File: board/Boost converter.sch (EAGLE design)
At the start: 21 parts, among them IC1 NE555N, IC2 attiny84, IC3 attiny85, Q1 2n7000, Q2 zvp4105

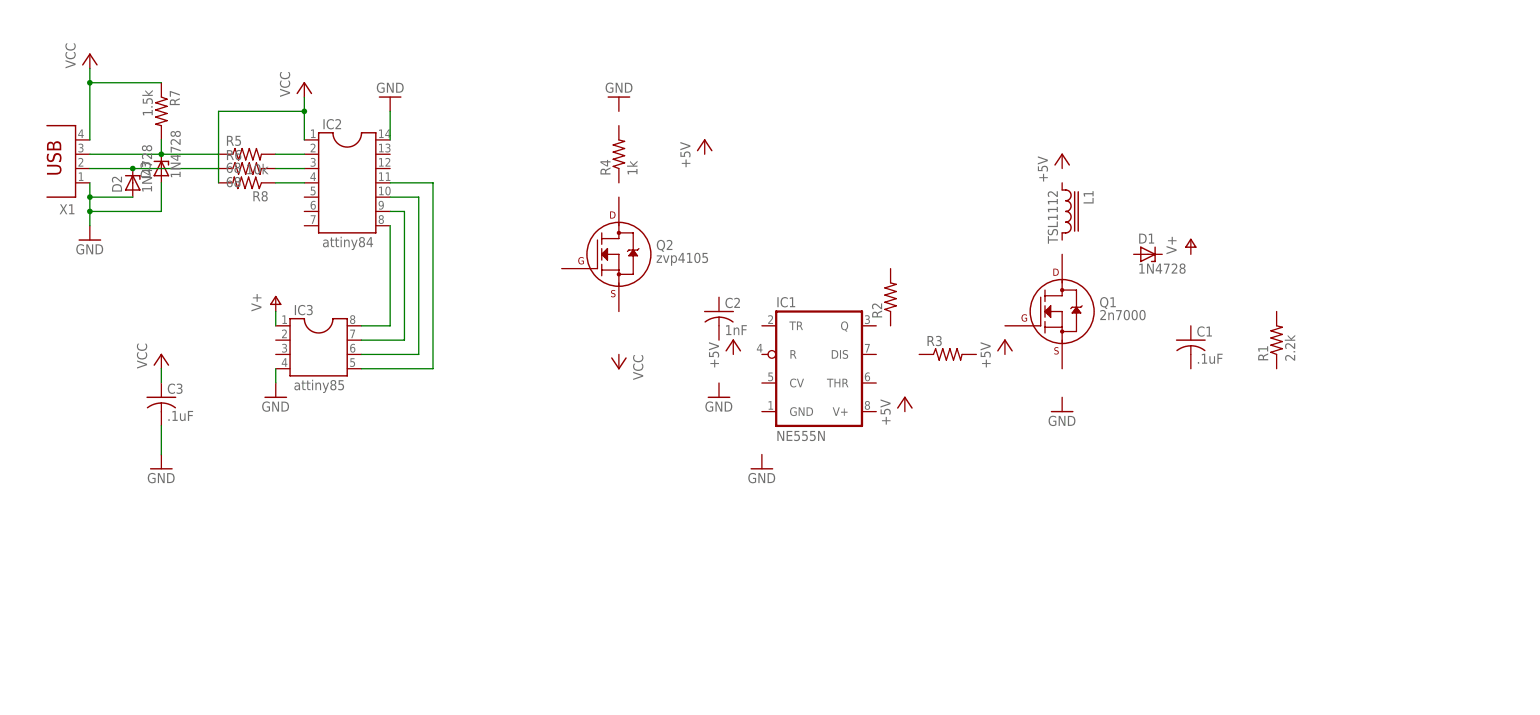
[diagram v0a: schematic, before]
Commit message: added v-usb library and done routing board
added v-usb library, but still need to change settings in usbconfig.h. also usb needs to use only one port for both d+ and d- lines (d+ can't be on pa0 and d- on pb1) so I had to change the usb data lines again. d+ is on PA0 with pcint0 and d- is on PA7. attiny85 pin 2 is now on PA6
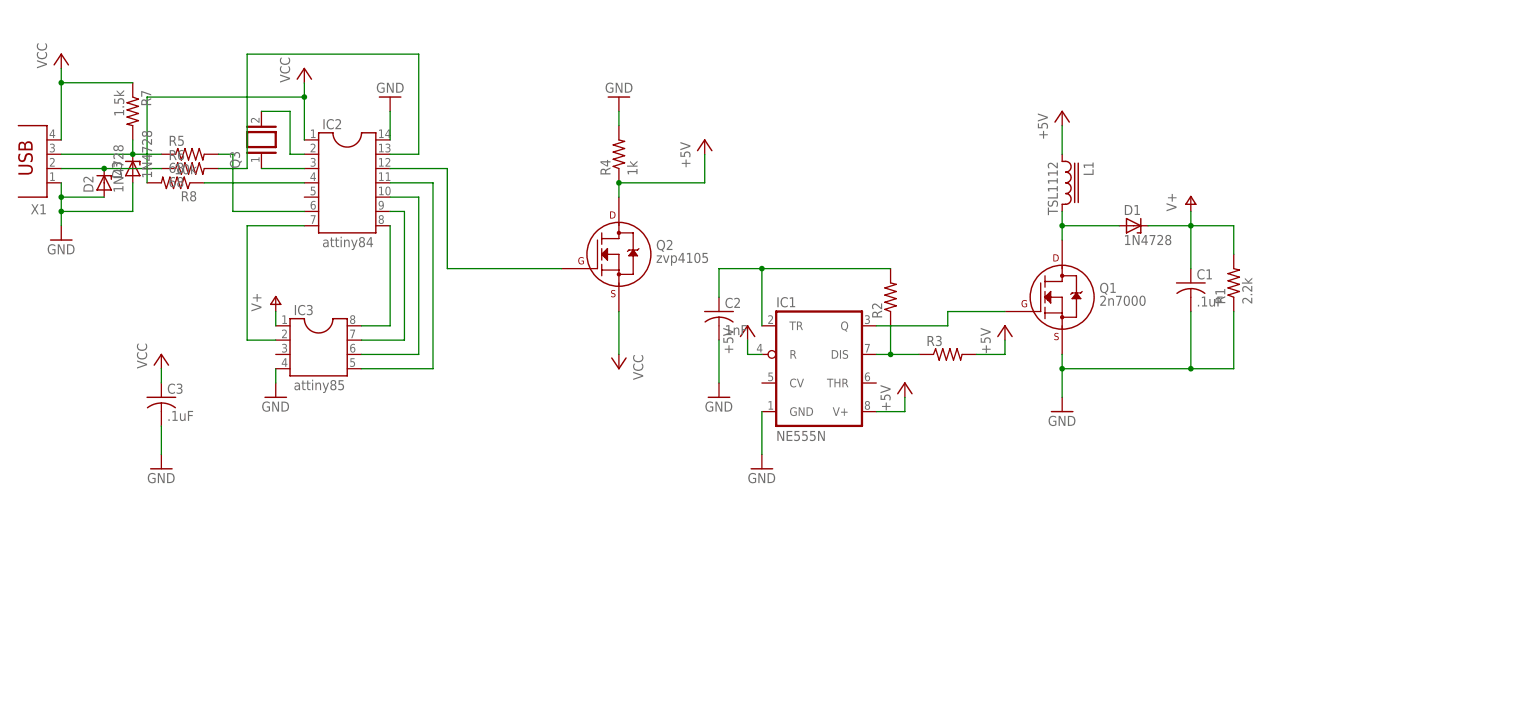
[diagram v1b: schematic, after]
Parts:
- added Q3: (no value), special:XTAL/S
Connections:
- new net +5V: IC1.R, IC1.V+, L1.1, Q2.D, R3.2, R4.1
- new net N$10: IC2.12, Q2.G
- new net N$11: IC2.2, Q3.2
- new net N$12: IC1.DIS, R2.1, R3.1
- new net N$13: C2.1, IC1.TR, R2.2
- new net N$14: IC1.Q, Q1.G
- new net N$15: D1.A, L1.2, Q1.D
- new net N$16: IC2.6, R5.2
- new net N$17: IC2.7, IC3.2
- net GND: now also C1.2, C2.2, IC1.GND, Q1.S, R1.1, R4.2
- net N$4: now also IC2.13, R6.2; no longer IC2.2, R5.2
- net N$5: now also Q3.1; no longer R6.2
- net V+: now also C1.1, D1.C, R1.2
- net VCC: now also Q2.S
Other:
- moved on the sheet: C1, D1, D2, D3, L1, Q1, R1, R5, R6, R7, R8, X1

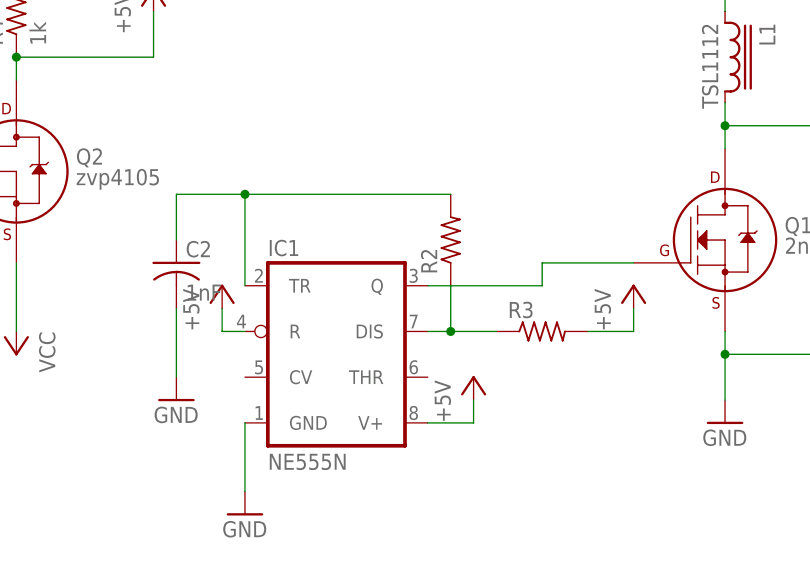
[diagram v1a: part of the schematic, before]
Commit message: Added crystal oscillator and potentiometer to board
crystal oscillator is next to ATtiny84 and potentiometer is next to inductor and 555. also moved around boost converter components so they are located in the same places as in the first version of the board. I should double check potentiometer sizes before having this board manufactured. Also should probably double check calculations and test current board with same signal diode and potentiometer to see actual range vs calculated range of output voltage
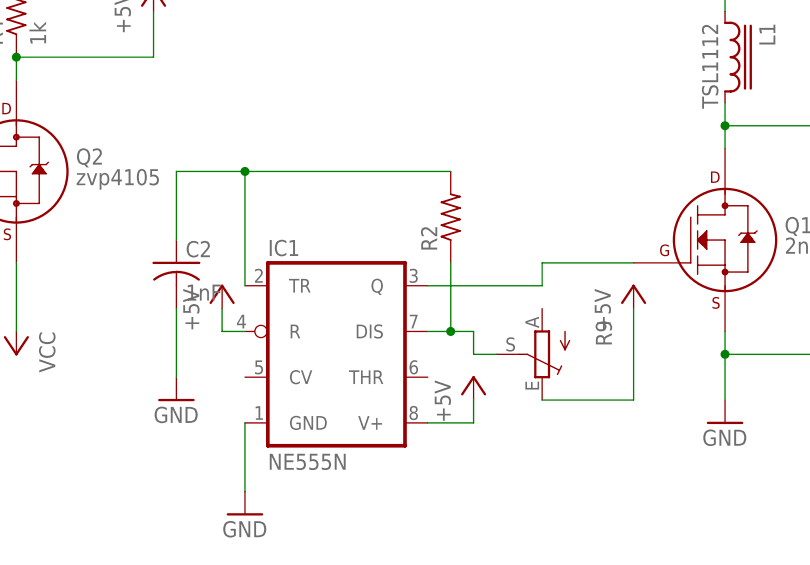
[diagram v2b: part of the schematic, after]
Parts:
- removed R3: (no value), resistor:R-US_0204/7
- added R9: (no value), pot:TRIM_EU-B25U
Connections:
- removed net N$12: IC1.DIS, R2.1, R3.1
- new net N$18: IC1.DIS, R2.1, R9.S
- net +5V: now also R9.E; no longer R3.2
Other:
- moved on the sheet: R2
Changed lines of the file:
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@@
 <part name="R1" library="resistor" deviceset="R-US_" device="0204/7" value="2.2k"/>
 <part name="R2" library="resistor" deviceset="R-US_" device="0204/7"/>
-<part name="R3" library="resistor" deviceset="R-US_" device="0204/7"/>
 <part name="R4" library="resistor" deviceset="R-US_" device="0204/7" value="1k"/>
 <part name="D1" library="diode" deviceset="1N4728" device=""/>
@@
 <part name="P+12" library="supply1" deviceset="V+" device=""/>
 <part name="Q3" library="special" deviceset="XTAL/S" device=""/>
+<part name="R9" library="pot" deviceset="TRIM_EU-" device="B25U"/>
 </parts>
 <sheets>
@@
 <instance part="C2" gate="G$1" x="58.42" y="63.5"/>
 <instance part="R1" gate="G$1" x="149.86" y="68.58" rot="R90"/>
-<instance part="R2" gate="G$1" x="88.9" y="66.04" rot="R90"/>
-<instance part="R3" gate="G$1" x="99.06" y="55.88"/>
+<instance part="R2" gate="G$1" x="88.9" y="68.58" rot="R90"/>
 <instance part="R4" gate="G$1" x="40.64" y="91.44" rot="R90"/>
 <instance part="D1" gate="1" x="132.08" y="78.74"/>
@@
 <instance part="P+12" gate="1" x="-20.32" y="66.04"/>
 <instance part="Q3" gate="G$1" x="-22.86" y="93.98" rot="R90"/>
+<instance part="R9" gate="1" x="99.06" y="53.34" rot="R180"/>
 </instances>
 <busses>
@@
 </segment>
 <segment>
-<pinref part="P+4" gate="1" pin="+5V"/>
-<wire x1="109.22" y1="58.42" x2="109.22" y2="55.88" width="0.1524" layer="91"/>
-<pinref part="R3" gate="G$1" pin="2"/>
-<wire x1="109.22" y1="55.88" x2="104.14" y2="55.88" width="0.1524" layer="91"/>
-</segment>
-<segment>
 <pinref part="P+3" gate="1" pin="+5V"/>
 <wire x1="63.5" y1="58.42" x2="63.5" y2="55.88" width="0.1524" layer="91"/>
@@
 <wire x1="119.38" y1="91.44" x2="119.38" y2="96.52" width="0.1524" layer="91"/>
 </segment>
-</net>
-<net name="N$12" class="0">
-<segment>
-<pinref part="R3" gate="G$1" pin="1"/>
-<pinref part="IC1" gate="A" pin="DIS"/>
-<wire x1="93.98" y1="55.88" x2="88.9" y2="55.88" width="0.1524" layer="91"/>
-<pinref part="R2" gate="G$1" pin="1"/>
-<wire x1="88.9" y1="55.88" x2="86.36" y2="55.88" width="0.1524" layer="91"/>
-<wire x1="88.9" y1="60.96" x2="88.9" y2="55.88" width="0.1524" layer="91"/>
-<junction x="88.9" y="55.88"/>
+<segment>
+<pinref part="R9" gate="1" pin="E"/>
+<wire x1="99.06" y1="48.26" x2="109.22" y2="48.26" width="0.1524" layer="91"/>
+<pinref part="P+4" gate="1" pin="+5V"/>
+<wire x1="109.22" y1="48.26" x2="109.22" y2="58.42" width="0.1524" layer="91"/>
 </segment>
 </net>
@@
 <pinref part="R2" gate="G$1" pin="2"/>
 <pinref part="IC1" gate="A" pin="TR"/>
-<wire x1="88.9" y1="71.12" x2="66.04" y2="71.12" width="0.1524" layer="91"/>
-<wire x1="66.04" y1="71.12" x2="66.04" y2="60.96" width="0.1524" layer="91"/>
+<wire x1="88.9" y1="73.66" x2="66.04" y2="73.66" width="0.1524" layer="91"/>
+<wire x1="66.04" y1="73.66" x2="66.04" y2="60.96" width="0.1524" layer="91"/>
 <pinref part="C2" gate="G$1" pin="1"/>
-<wire x1="66.04" y1="71.12" x2="58.42" y2="71.12" width="0.1524" layer="91"/>
-<wire x1="58.42" y1="71.12" x2="58.42" y2="66.04" width="0.1524" layer="91"/>
-<junction x="66.04" y="71.12"/>
+<wire x1="66.04" y1="73.66" x2="58.42" y2="73.66" width="0.1524" layer="91"/>
+<wire x1="58.42" y1="73.66" x2="58.42" y2="66.04" width="0.1524" layer="91"/>
+<junction x="66.04" y="73.66"/>
 </segment>
 </net>
@@
 </segment>
 </net>
+<net name="N$18" class="0">
+<segment>
+<pinref part="R9" gate="1" pin="S"/>
+<wire x1="93.98" y1="53.34" x2="91.44" y2="53.34" width="0.1524" layer="91"/>
+<wire x1="91.44" y1="53.34" x2="91.44" y2="55.88" width="0.1524" layer="91"/>
+<pinref part="IC1" gate="A" pin="DIS"/>
+<wire x1="91.44" y1="55.88" x2="88.9" y2="55.88" width="0.1524" layer="91"/>
+<pinref part="R2" gate="G$1" pin="1"/>
+<wire x1="88.9" y1="55.88" x2="86.36" y2="55.88" width="0.1524" layer="91"/>
+<wire x1="88.9" y1="63.5" x2="88.9" y2="55.88" width="0.1524" layer="91"/>
+<junction x="88.9" y="55.88"/>
+</segment>
+</net>

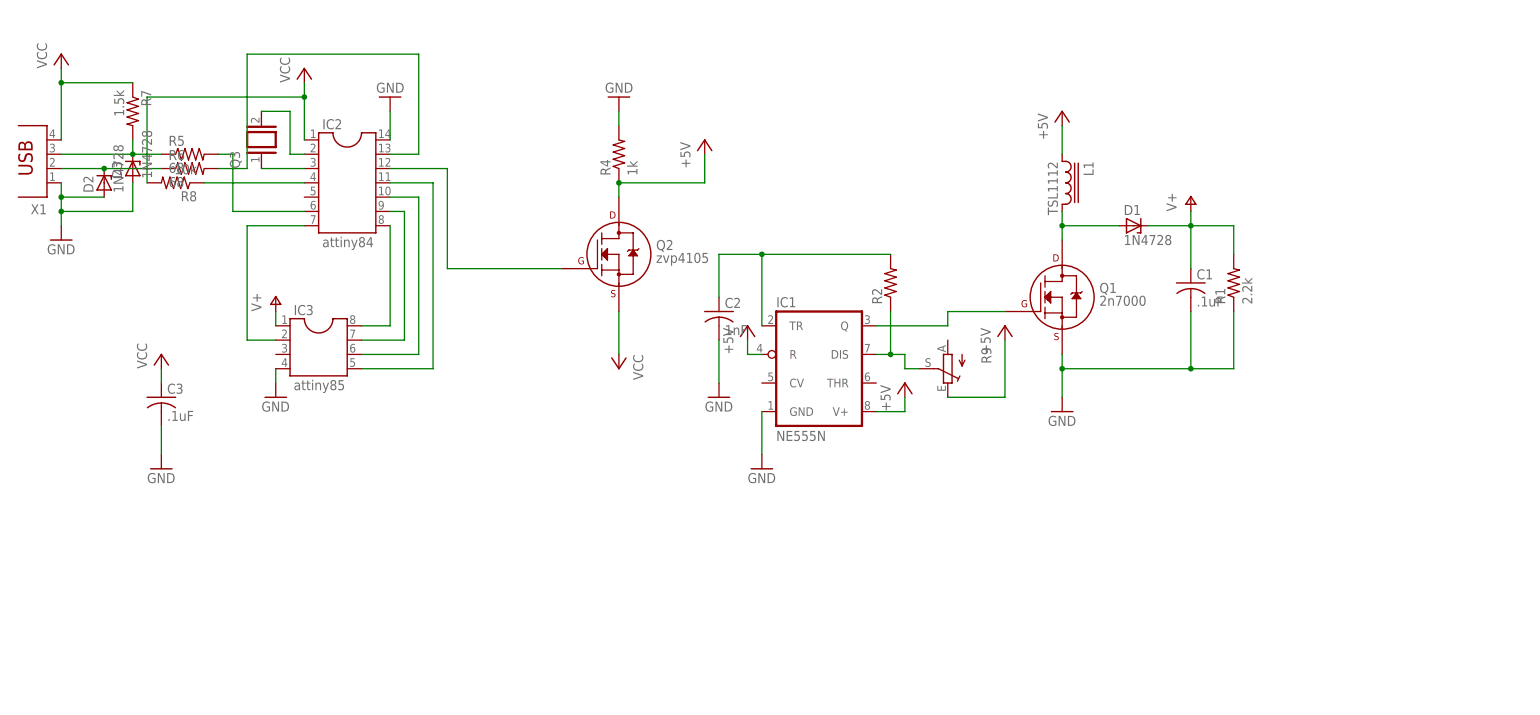
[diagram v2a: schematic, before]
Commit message: Board Version 2
Updated board to include crystal oscillator and caps, boost converter feedback loop with resistor divider and mosfet inverter to trigger 555 reset pin and cmos for supplying 12V to t85 reset pin. Dimensions also changed to 1.4" by 2" to accomodate the new components
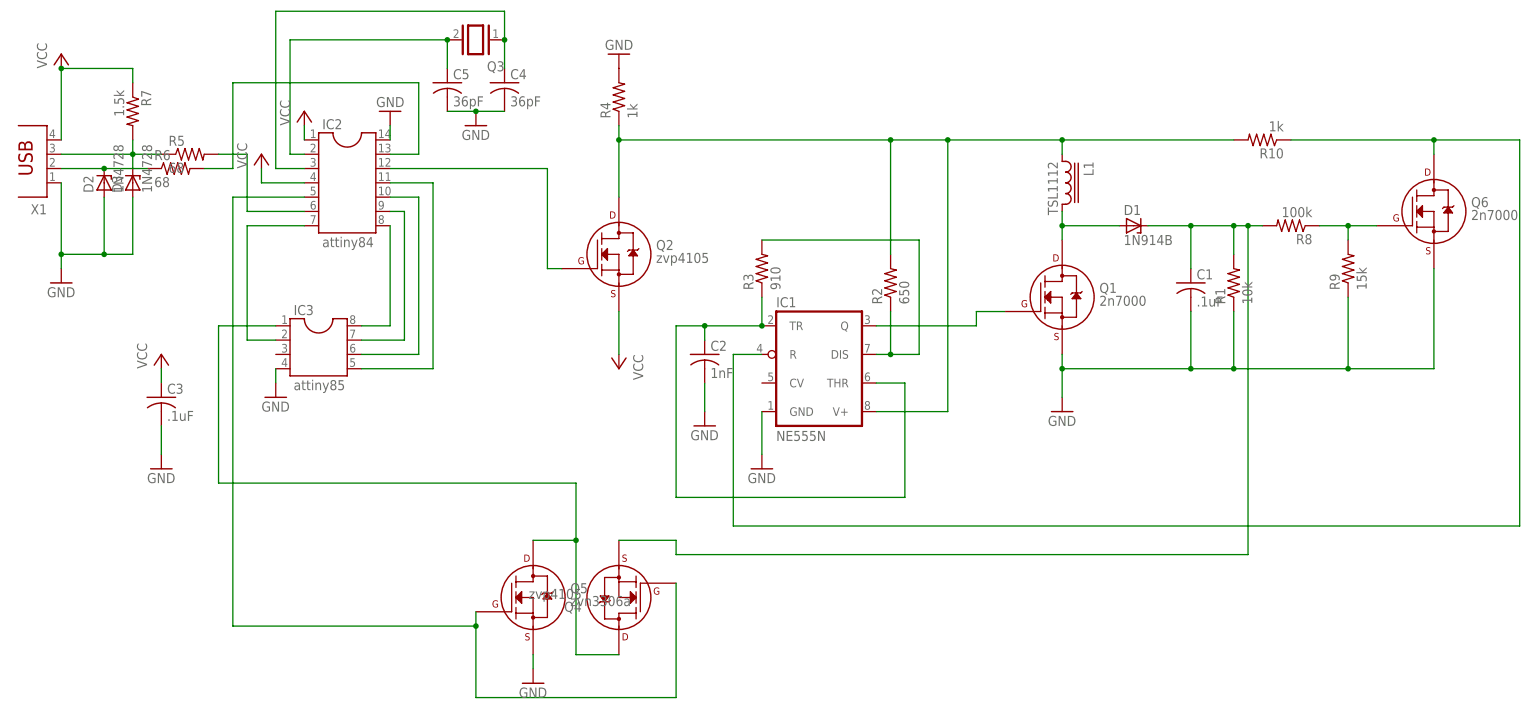
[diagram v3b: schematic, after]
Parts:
- added C4, C5: 36pF, resistor:C-US025-024X044
- added Q4: zvp4105, transistor2:2N7000_TO92
- added Q5: zvn3306a, transistor2:2N7000_TO92
- added Q6: 2n7000, transistor2:2N7000_TO92
- added R10: 1k, resistor:R-US_0204/7
- added R3: 910, resistor:R-US_0204/7
- D1: value 1N4728 -> 1N914B
- R1: value 2.2k -> 10k
- R2: value (none) -> 650
- R8: value 10k -> 100k
- R9: value (none) -> 15k; device pot:TRIM_EU-B25U -> resistor:R-US_0204/7
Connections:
- removed net +5V: IC1.R, IC1.V+, L1.1, Q2.D, R4.1, R9.E
- removed net N$1 (its old number): IC2.4, R8.1
- removed net N$18: IC1.DIS, R2.1, R9.S
- removed net N$5 (its old number): IC2.3, Q3.1
- removed net V+: C1.1, D1.C, IC3.1, R1.2
- new net N$14: C2.1, IC1.THR, IC1.TR, R3.1
- new net N$16: IC3.1, Q4.D, Q5.D
- new net N$17: IC2.5, Q4.G, Q5.G
- new net N$2: C5.1, IC2.2, Q3.2
- new net N$3: C4.1, IC2.3, Q3.1
- new net N$7: IC1.V+, L1.1, Q2.D, R10.2, R2.2, R4.1
- new net N$8: Q6.G, R8.1, R9.2
- new net N$9: IC1.R, Q6.D, R10.1
- net GND: now also C4.2, C5.2, Q5.S, Q6.S, R9.1
- net N$11: now also C1.1, D1.C, Q4.S, R1.2, R8.2; no longer IC2.2, Q3.2
- net N$13: now also IC1.DIS, R2.1, R3.2; no longer C2.1, IC1.TR, R2.2
- net VCC: now also IC2.4; no longer R8.2
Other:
- moved on the sheet: C2, D3, Q3, R4, R6, R8
